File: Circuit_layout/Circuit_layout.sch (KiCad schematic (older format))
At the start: 32 parts, among them SW1 SW_PUSH, U15 TLP293, U17 MCP6004, U7 AT90CAN128-A, U9 TLP293, Y1 10MHz

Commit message: fixing nets. most done except for GND/driving issue
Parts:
- W1, W2, W3: footprint (none) -> Measurement_Points:Measurement_Point_Round-SMD-Pad_Big
- gave numbers to parts that had none: 1
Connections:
- net labels added: PIN54, PIN55
- wire segments 131 -> 137
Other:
- moved on the sheet: R43, SW3

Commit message: current sensor enable
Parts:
- added Q3: MMBF170, TO_SOT_Packages_SMD:SOT-23, symbol MMBF170
- added R14, R18, R8: 10k, Resistors_SMD:R_0805_HandSoldering, symbol R
- R2: value 10k -> 250k; Cost (none) -> 0.10; Description (none) -> RES SMD 249K OHM 1% 1/8W 0805; DigiKey P/N P10.0KCCT-ND -> P249KCCT-ND; Man P/N ERJ-6ENF1002V -> ERJ-6ENF2493V; URL http://www.digikey.com/product-detail/en/panasonic-electronic-components/ERJ-6ENF1002V/P10.0KCCT-ND/119248 -> http://www.digikey.com/product-detail/en/panasonic-electronic-components/ERJ-6ENF2493V/P249KCCT-ND/119664
- SW1: footprint (none) -> custom_footprints:SW_RACON_8; Cost (none) -> 2.40; Description (none) -> SWITCH PUSH SPST-NO 0.1A 42V; DigiKey P/N (none) -> 1715-1676-1-ND; Man P/N (none) -> 1.14100.5030000; URL (none) -> http://www.digikey.com/products/en?keywords=ckn9363ct-nd
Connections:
- net labels added: I_+5, I_ENB, I_RTN
- wire segments 137 -> 151
- no-connect marks 25 -> 24
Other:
- note added: "Current Enable"
- note added: "Increased the R on AIRs to match pullups of of BP, BOT to limit current"
- note added: "Spare ADC Switch"
- note added: "TSV has extras of these (SW)"
- moved on the sheet: C1, C2, C25, C31, C4, C5, C6, C7, R1, R10, R11, R13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

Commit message: modifying hvpl
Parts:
- U7: symbol AT90CAN128-A -> AT90CAN128-A-RESCUE-Circuit_layout
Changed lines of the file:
@@
 LIBS:xilinx
 LIBS:Zilog
-LIBS:pacman-main-cache
 LIBS:bss84
 LIBS:+10v
@@
 $EndDescr
 $Comp
-L AT90CAN128-A U7
+L AT90CAN128-A-RESCUE-Circuit_layout U7
 U 1 1 58A74D86
 P 8500 3500

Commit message: added footprint to DPDT switch, test points, DRC passes
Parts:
- SW3: footprint (none) -> custom_footprints:CK_DPDT_Switch
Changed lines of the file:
@@
 LIBS:xilinx
 LIBS:Zilog
+LIBS:pacman-main-cache
 LIBS:bss84
 LIBS:+10v
@@
 F 0 "SW3" H 12850 1700 50  0000 C CNN
 F 1 "JS202011CQN" H 13000 1600 50  0000 C CNN
-F 2 "" H 12550 2200 50  0001 C CNN
+F 2 "custom_footprints:CK_DPDT_Switch" H 12550 2200 50  0001 C CNN
 F 3 "http://www.ckswitches.com/media/1422/js.pdf" H 12550 2200 50  0001 C CNN
 F 4 "401-2001-ND" H 12550 2200 60  0001 C CNN "DigiKey P/N"

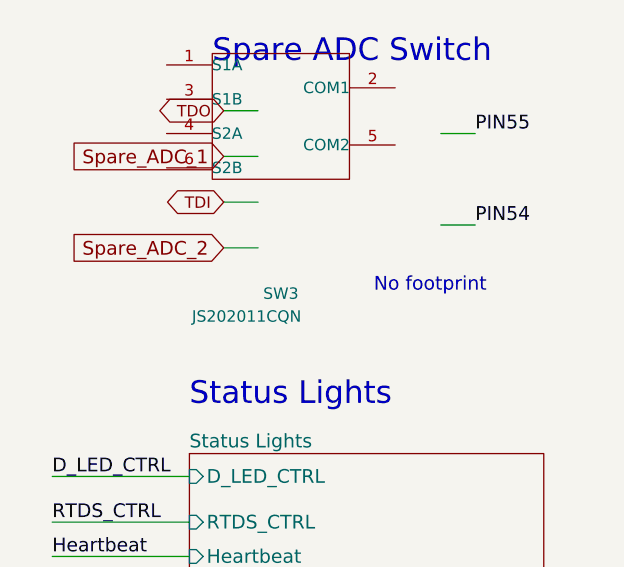
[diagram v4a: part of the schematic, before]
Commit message: cleaned up footprints of more testpoints. ran DRC again, passed
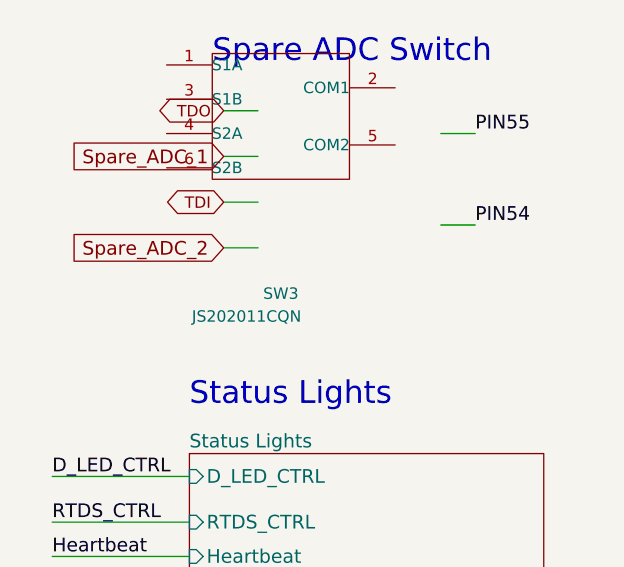
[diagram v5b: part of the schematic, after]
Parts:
- W3: footprint Measurement_Points:Measurement_Point_Round-SMD-Pad_Big -> Measurement_Points:Measurement_Point_Square-SMD-Pad_Big
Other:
- note removed: "No footprint"
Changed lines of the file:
@@
 F 0 "W3" H 8200 6170 50  0000 C CNN
 F 1 "uC_GND" H 8200 6100 50  0000 C CNN
-F 2 "Measurement_Points:Measurement_Point_Round-SMD-Pad_Big" H 8400 5900 50  0001 C CNN
+F 2 "Measurement_Points:Measurement_Point_Square-SMD-Pad_Big" H 8400 5900 50  0001 C CNN
 F 3 "" H 8400 5900 50  0000 C CNN
 	1    8200 5900
@@
 Text GLabel 12000 2500 0    60   Input ~ 0
 Spare_ADC_2
-Text Notes 13150 2700 2    60   ~ 0
-No footprint
 Text Notes 9800 -400 0    60   ~ 0
 NOTE: Add footprints to test points (already in lib)

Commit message: reviewed schematic w/ prof. nadovich. proposed changes
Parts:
- removed C1, C2: 0.1u, Capacitors_SMD:C_0805_HandSoldering, symbol C
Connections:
- wire segments 151 -> 147
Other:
- note added: "Make R9 660K or greater"
- note added: "Make this a better symbol\ni.e. box with I/O pin numbers + names"
- note added: "Remove this, alter gain on R9 to make 24V-5V"
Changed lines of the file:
@@
-$EndComp
-$Comp
-L GND #PWR04
-U 1 1 58B23714
-P 1350 6000
-F 0 "#PWR04" H 1350 5750 50  0001 C CNN
-F 1 "GND" H 1350 5850 50  0000 C CNN
-F 2 "" H 1350 6000 50  0000 C CNN
-F 3 "" H 1350 6000 50  0000 C CNN
-	1    1350 6000
-	1    0    0    -1
 $EndComp
 $Comp
 L GND #PWR05
 U 1 1 58B237F4
-P 1000 4800
-F 0 "#PWR05" H 1000 4550 50  0001 C CNN
-F 1 "GND" H 1000 4650 50  0000 C CNN
-F 2 "" H 1000 4800 50  0000 C CNN
-F 3 "" H 1000 4800 50  0000 C CNN
-	1    1000 4800
+P 1800 4850
+F 0 "#PWR05" H 1800 4600 50  0001 C CNN
+F 1 "GND" H 1800 4700 50  0000 C CNN
+F 2 "" H 1800 4850 50  0000 C CNN
+F 3 "" H 1800 4850 50  0000 C CNN
+	1    1800 4850
 	1    0    0    -1
 $EndComp
@@
 F 6 "MCP6004T-I/SL" H 2400 5400 60  0001 C CNN "Man P/N"
 	1    2400 5400
-	1    0    0    -1
-$EndComp
-$Comp
-L C C2
-U 1 1 58B40314
-P 1350 5800
-F 0 "C2" H 1375 5900 50  0000 L CNN
-F 1 "0.1u" H 1375 5700 50  0000 L CNN
-F 2 "Capacitors_SMD:C_0805_HandSoldering" H 1388 5650 50  0001 C CNN
-F 3 "http://www.kemet.com/Lists/ProductCatalog/Attachments/53/KEM_C1002_X7R_SMD.pdf" H 1350 5800 50  0001 C CNN
-F 4 "399-1168-1-ND" H 1350 5800 60  0001 C CNN "Digikey P/N"
-F 5 "http://www.digikey.com/product-detail/en/kemet/C0805C104K3RACTU/399-1168-1-ND/411443" H 1350 5800 60  0001 C CNN "URL"
-F 6 "C0805C104K3RACTU" H 1350 5800 60  0001 C CNN "Man P/N"
-	1    1350 5800
-	1    0    0    -1
-$EndComp
-$Comp
-L C C1
-U 1 1 58B40445
-P 1350 5000
-F 0 "C1" H 1375 5100 50  0000 L CNN
-F 1 "0.1u" H 1375 4900 50  0000 L CNN
-F 2 "Capacitors_SMD:C_0805_HandSoldering" H 1388 4850 50  0001 C CNN
-F 3 "http://www.kemet.com/Lists/ProductCatalog/Attachments/53/KEM_C1002_X7R_SMD.pdf" H 1350 5000 50  0001 C CNN
-F 4 "399-1168-1-ND" H 1350 5000 60  0001 C CNN "Digikey P/N"
-F 5 "http://www.digikey.com/product-detail/en/kemet/C0805C104K3RACTU/399-1168-1-ND/411443" H 1350 5000 60  0001 C CNN "URL"
-F 6 "C0805C104K3RACTU" H 1350 5000 60  0001 C CNN "Man P/N"
-	1    1350 5000
 	1    0    0    -1
 $EndComp
@@
 	1850 5300 2100 5300
 Wire Wire Line
-	1350 5300 1350 5150
-Connection ~ 1350 5300
-Wire Wire Line
-	1350 5650 1350 5500
-Connection ~ 1350 5500
-Wire Wire Line
-	1000 4700 2000 4700
-Wire Wire Line
-	1350 4700 1350 4850
-Wire Wire Line
 	2000 5300 2000 5150
 Connection ~ 2000 5300
 Wire Wire Line
-	2000 4700 2000 4850
-Connection ~ 1350 4700
-Wire Wire Line
 	9800 3700 10450 3700
 Wire Wire Line
@@
 Wire Wire Line
 	2750 6000 2500 6000
-Wire Wire Line
-	1350 5950 1350 6000
 Wire Wire Line
 	9800 3300 10450 3300
@@
 Wire Wire Line
 	4700 2950 4700 2800
-Wire Wire Line
-	1000 4800 1000 4700
 Wire Wire Line
 	1100 3200 1700 3200
@@
 Wire Wire Line
 	9800 2500 10150 2500
+Text Notes 1100 4050 0    60   ~ 0
+Remove this, alter gain on R9 to make 24V-5V
+Text Notes 13750 2200 0    60   ~ 0
+Make this a better symbol\ni.e. box with I/O pin numbers + names
+Wire Wire Line
+	1800 4850 1800 4750
+Wire Wire Line
+	1800 4750 2000 4750
+Wire Wire Line
+	2000 4750 2000 4850
+Text Notes 2400 3500 0    60   ~ 0
+Make R9 660K or greater
 $EndSCHEMATC

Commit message: small changes
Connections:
- net labels removed: I_+5
- wire segments 147 -> 145
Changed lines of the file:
@@
 $EndComp
 $Comp
-L GND #PWR05
+L GND #PWR04
 U 1 1 58B237F4
 P 1800 4850
-F 0 "#PWR05" H 1800 4600 50  0001 C CNN
+F 0 "#PWR04" H 1800 4600 50  0001 C CNN
 F 1 "GND" H 1800 4700 50  0000 C CNN
 F 2 "" H 1800 4850 50  0000 C CNN
@@
 $EndComp
 $Comp
-L +5V #PWR06
+L +5V #PWR05
 U 1 1 58B238C3
 P 2300 5000
-F 0 "#PWR06" H 2300 4850 50  0001 C CNN
+F 0 "#PWR05" H 2300 4850 50  0001 C CNN
 F 1 "+5V" H 2300 5140 50  0000 C CNN
 F 2 "" H 2300 5000 50  0000 C CNN
@@
 $EndComp
 $Comp
-L GND #PWR07
+L GND #PWR06
 U 1 1 58B84EB4
 P 7050 2900
-F 0 "#PWR07" H 7050 2650 50  0001 C CNN
+F 0 "#PWR06" H 7050 2650 50  0001 C CNN
 F 1 "GND" H 7050 2750 50  0000 C CNN
 F 2 "" H 7050 2900 50  0000 C CNN
@@
 $EndComp
 $Comp
-L +5V #PWR08
+L +5V #PWR07
 U 1 1 58B98E0E
 P 3600 5050
-F 0 "#PWR08" H 3600 4900 50  0001 C CNN
+F 0 "#PWR07" H 3600 4900 50  0001 C CNN
 F 1 "+5V" H 3600 5190 50  0000 C CNN
 F 2 "" H 3600 5050 50  0000 C CNN
@@
 $EndComp
 $Comp
-L GND #PWR09
+L GND #PWR08
 U 1 1 58B99168
 P 3600 5650
-F 0 "#PWR09" H 3600 5400 50  0001 C CNN
+F 0 "#PWR08" H 3600 5400 50  0001 C CNN
 F 1 "GND" H 3600 5500 50  0000 C CNN
 F 2 "" H 3600 5650 50  0000 C CNN
@@
 Intended for 10Hz PWM\ntau=6.345s
 $Comp
-L +5V #PWR010
+L +5V #PWR09
 U 1 1 58BBB92E
 P 3700 2450
-F 0 "#PWR010" H 3700 2300 50  0001 C CNN
+F 0 "#PWR09" H 3700 2300 50  0001 C CNN
 F 1 "+5V" H 3700 2590 50  0000 C CNN
 F 2 "" H 3700 2450 50  0000 C CNN
@@
 $EndComp
 $Comp
-L GND #PWR011
+L GND #PWR010
 U 1 1 58BBB934
 P 3700 3450
-F 0 "#PWR011" H 3700 3200 50  0001 C CNN
+F 0 "#PWR010" H 3700 3200 50  0001 C CNN
 F 1 "GND" H 3700 3300 50  0000 C CNN
 F 2 "" H 3700 3450 50  0000 C CNN
@@
 $EndComp
 $Comp
-L +5V #PWR012
+L +5V #PWR011
 U 1 1 58BC98C5
 P 4700 2800
-F 0 "#PWR012" H 4700 2650 50  0001 C CNN
+F 0 "#PWR011" H 4700 2650 50  0001 C CNN
 F 1 "+5V" H 4700 2940 50  0000 C CNN
 F 2 "" H 4700 2800 50  0000 C CNN
@@
 $EndComp
 $Comp
-L GND #PWR013
+L GND #PWR012
 U 1 1 58BC98CB
 P 4700 3400
-F 0 "#PWR013" H 4700 3150 50  0001 C CNN
+F 0 "#PWR012" H 4700 3150 50  0001 C CNN
 F 1 "GND" H 4700 3250 50  0000 C CNN
 F 2 "" H 4700 3400 50  0000 C CNN
@@
 $EndComp
 $Comp
-L GND #PWR014
+L GND #PWR013
 U 1 1 58BB75AC
 P 2850 1650
-F 0 "#PWR014" H 2850 1400 50  0001 C CNN
+F 0 "#PWR013" H 2850 1400 50  0001 C CNN
 F 1 "GND" H 2850 1500 50  0000 C CNN
 F 2 "" H 2850 1650 50  0000 C CNN
@@
 $EndComp
 $Comp
-L GND #PWR015
+L GND #PWR014
 U 1 1 58BB7DFB
 P 2350 4050
-F 0 "#PWR015" H 2350 3800 50  0001 C CNN
+F 0 "#PWR014" H 2350 3800 50  0001 C CNN
 F 1 "GND" H 2350 3900 50  0000 C CNN
 F 2 "" H 2350 4050 50  0000 C CNN
@@
 $EndComp
 $Comp
-L +5V #PWR016
+L +5V #PWR015
 U 1 1 58BBF1E9
 P 2350 2650
-F 0 "#PWR016" H 2350 2500 50  0001 C CNN
+F 0 "#PWR015" H 2350 2500 50  0001 C CNN
 F 1 "+5V" H 2350 2790 50  0000 C CNN
 F 2 "" H 2350 2650 50  0000 C CNN
@@
 Isolator used to move \n24V PWM to 5V PWM for uC
 $Comp
-L PWR_FLAG #FLG017
+L PWR_FLAG #FLG016
 U 1 1 58BDECDC
 P 2700 2700
-F 0 "#FLG017" H 2700 2795 50  0001 C CNN
+F 0 "#FLG016" H 2700 2795 50  0001 C CNN
 F 1 "PWR_FLAG" H 2700 2880 50  0000 C CNN
 F 2 "" H 2700 2700 50  0000 C CNN
@@
 $EndComp
 $Comp
-L +5V #PWR018
+L +5V #PWR017
 U 1 1 58BE6C42
 P 10500 5950
-F 0 "#PWR018" H 10500 5800 50  0001 C CNN
+F 0 "#PWR017" H 10500 5800 50  0001 C CNN
 F 1 "+5V" H 10500 6090 50  0000 C CNN
 F 2 "" H 10500 5950 50  0000 C CNN
@@
 ~RESET_AVR
 $Comp
-L +5V #PWR019
+L +5V #PWR018
 U 1 1 58C14221
 P 3650 1100
-F 0 "#PWR019" H 3650 950 50  0001 C CNN
+F 0 "#PWR018" H 3650 950 50  0001 C CNN
 F 1 "+5V" H 3650 1240 50  0000 C CNN
 F 2 "" H 3650 1100 50  0000 C CNN
@@
 ~RESET_AVR
 $Comp
-L GND #PWR020
+L GND #PWR019
 U 1 1 58BFFF85
 P 4850 1650
-F 0 "#PWR020" H 4850 1400 50  0001 C CNN
+F 0 "#PWR019" H 4850 1400 50  0001 C CNN
 F 1 "GND" H 4850 1500 50  0000 C CNN
 F 2 "" H 4850 1650 50  0000 C CNN
@@
 $EndComp
 $Comp
-L GND #PWR021
+L GND #PWR020
 U 1 1 58C35653
 P 3200 3700
-F 0 "#PWR021" H 3200 3450 50  0001 C CNN
+F 0 "#PWR020" H 3200 3450 50  0001 C CNN
 F 1 "GND" H 3200 3550 50  0000 C CNN
 F 2 "" H 3200 3700 50  0000 C CNN
@@
 $EndComp
 $Comp
-L GND #PWR022
+L GND #PWR021
 U 1 1 58D0C10E
 P 10600 1550
-F 0 "#PWR022" H 10600 1300 50  0001 C CNN
+F 0 "#PWR021" H 10600 1300 50  0001 C CNN
 F 1 "GND" H 10600 1400 50  0000 C CNN
 F 2 "" H 10600 1550 50  0000 C CNN
@@
 PIN54
 $Comp
-L GND #PWR023
+L GND #PWR022
 U 1 1 58D1DF35
 P 8450 5600
-F 0 "#PWR023" H 8450 5350 50  0001 C CNN
+F 0 "#PWR022" H 8450 5350 50  0001 C CNN
 F 1 "GND" H 8450 5450 50  0000 C CNN
 F 2 "" H 8450 5600 50  0000 C CNN
@@
 SDA
 $Comp
-L +5V #PWR024
+L +5V #PWR023
 U 1 1 58D09A18
 P 10500 6300
-F 0 "#PWR024" H 10500 6150 50  0001 C CNN
+F 0 "#PWR023" H 10500 6150 50  0001 C CNN
 F 1 "+5V" H 10500 6440 50  0000 C CNN
 F 2 "" H 10500 6300 50  0000 C CNN
@@
 Text GLabel 5300 5050 2    60   Input ~ 0
 I_RTN
-Text GLabel 5300 4750 2    60   Input ~ 0
-I_+5
-$Comp
-L +5V #PWR025
-U 1 1 58D13DFF
-P 5200 4650
-F 0 "#PWR025" H 5200 4500 50  0001 C CNN
-F 1 "+5V" H 5200 4790 50  0000 C CNN
-F 2 "" H 5200 4650 50  0000 C CNN
-F 3 "" H 5200 4650 50  0000 C CNN
-	1    5200 4650
-	1    0    0    -1
-$EndComp
 $Comp
 L R R14
@@
 $EndComp
 $Comp
-L GND #PWR026
+L GND #PWR025
 U 1 1 58D15ED8
 P 5200 5900
-F 0 "#PWR026" H 5200 5650 50  0001 C CNN
+F 0 "#PWR025" H 5200 5650 50  0001 C CNN
 F 1 "GND" H 5200 5750 50  0000 C CNN
 F 2 "" H 5200 5900 50  0000 C CNN
@@
 	5200 5050 5300 5050
 Wire Wire Line
-	5200 4650 5200 4750
-Wire Wire Line
-	5200 4750 5300 4750
-Wire Wire Line
 	4700 5400 4900 5400

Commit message: made changes discussed in sch review w/ prof. added back +5 plane
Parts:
- removed R27: 137k, Resistors_SMD:R_0805_HandSoldering, symbol R
- removed R5: 1k, Resistors_SMD:R_0805_HandSoldering, symbol R
- removed U15: TLP293, Housings_SSOP:SOP-4_4.4x2.8mm_Pitch1.27mm, symbol TLP291
- R1: value 10k -> 665k; Cost (none) -> 0.10; Description (none) -> RES SMD 665K OHM 1% 1/8W 0805; DigiKey P/N P10.0KCCT-ND -> P665KCCT-ND; Man P/N ERJ-6ENF1002V -> ERJ-6ENF6653V; URL http://www.digikey.com/product-detail/en/panasonic-electron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 -> https://www.digikey.com/product-detail/en/panasonic-electro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
- R9: value 137k -> 665k; Cost (none) -> 0.10; Description (none) -> RES SMD 665K OHM 1% 1/8W 0805; DigiKey P/N P137KCCT-ND -> P665KCCT-ND; Man P/N ERJ-6ENF1373V -> ERJ-6ENF6653V; URL http://www.digikey.com/product-detail/en/panasonic-electron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 -> https://www.digikey.com/product-detail/en/panasonic-electro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
- Y1: footprint Crystals:Crystal_SMD_HC49-SD_HandSoldering -> custom_footprints:crystal_TXC_7A; Cost (none) -> 0.66; Description (none) -> CRYSTAL 10.0000MHZ 12PF SMD; DigiKey P/N 535-9065-1-ND -> 887-1741-1-ND; Man P/N ABLS-10.000MHZ-B2-T -> 7A-10.000MAAE-T; URL http://www.digikey.com/product-detail/en/abracon-llc/ABLS-1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 -> https://www.digikey.com/products/en?pv7=2&k=7A-10.000MAAE-T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
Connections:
- wire segments 145 -> 135
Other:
- note added: "Gain intended to \nmove 24V to 5V range"
- note removed: "Isolator used to move \n24V PWM to 5V PWM for uC"
- note removed: "Make R9 660K or greater"
- note removed: "Make this a better symbol\ni.e. box with I/O pin numbers + names"
- note removed: "Remove this, alter gain on R9 to make 24V-5V"
- note removed: "TSV has extras of these (SW)"
- moved on the sheet: C4, C7, R10, R36, R9, SW3, U17B, W2
